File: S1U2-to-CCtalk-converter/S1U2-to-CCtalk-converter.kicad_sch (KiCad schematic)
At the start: 23 parts, among them J1 DB9_Female, J2 CCtalk Cable, J3 CCtalk Cable, Q1 BC847, Q2 BC856, U1 ST232B, U2 L7805

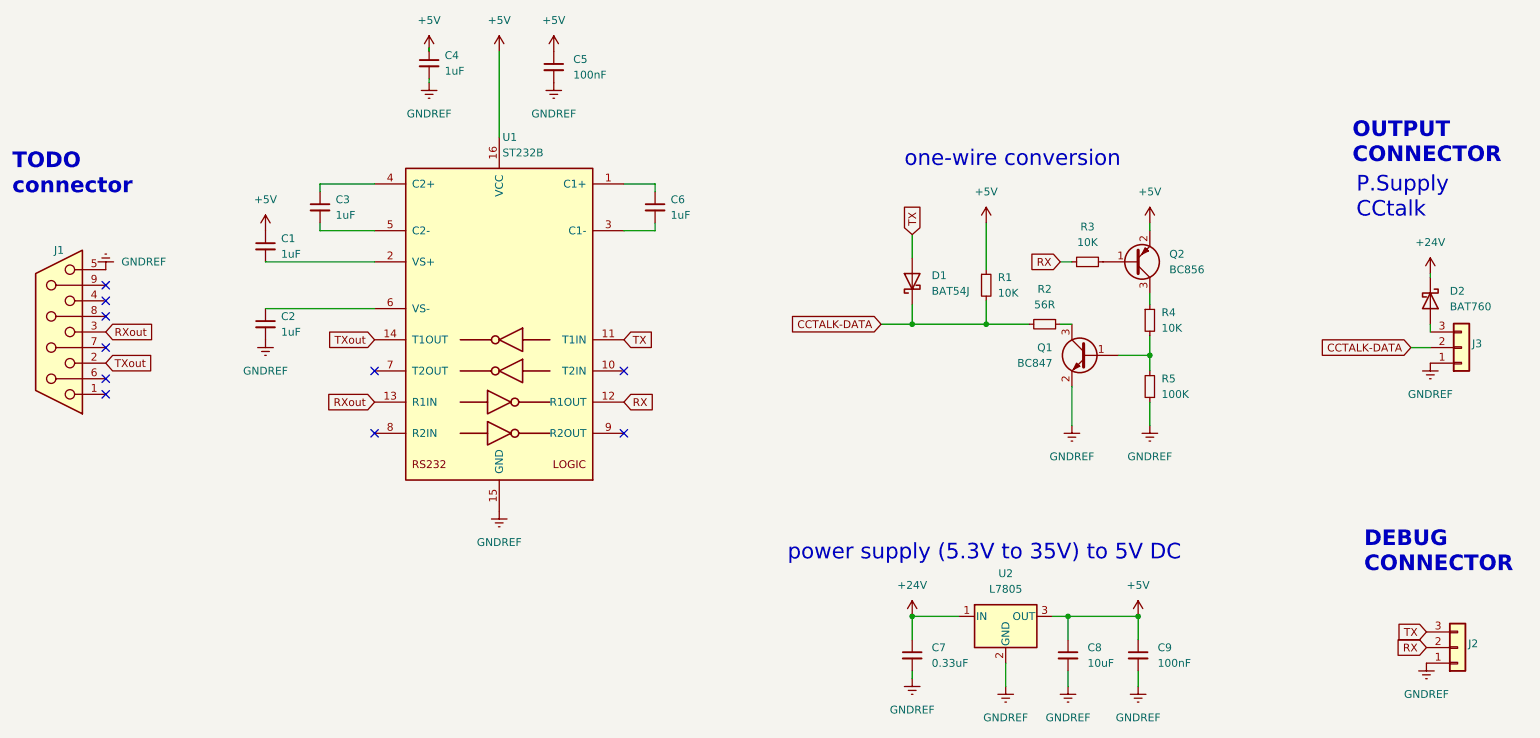
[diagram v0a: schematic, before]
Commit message: add s1u2 dxf bckg and place components
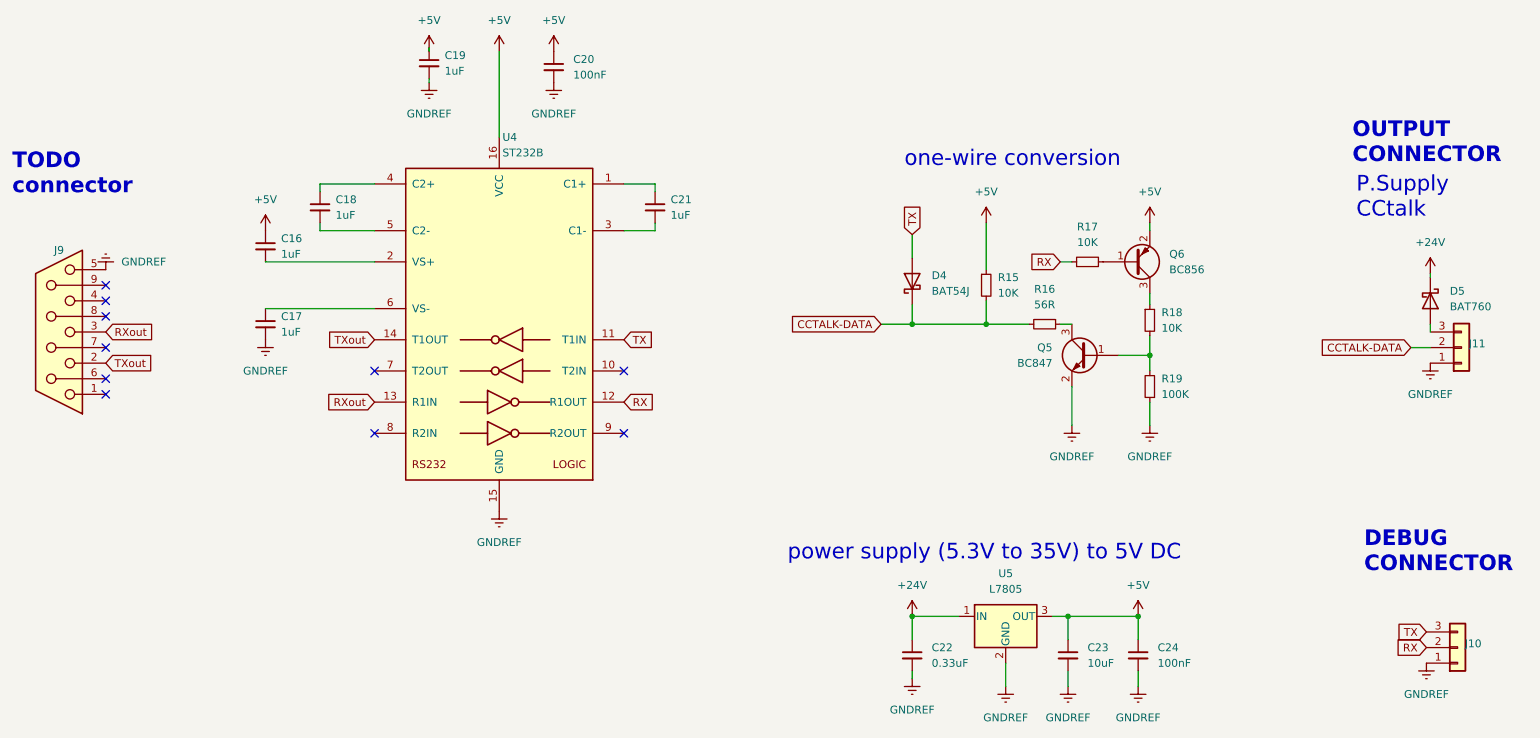
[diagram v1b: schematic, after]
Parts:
- renumbered C1 to C16, C2 to C17, C3 to C18, C4 to C19, C5 to C20, C6 to C21, C7 to C22, C8 to C23, C9 to C24, D1 to D4, D2 to D5, J2 to J10, J3 to J11, J1 to J9, Q1 to Q5, Q2 to Q6, R1 to R15, R2 to R16, R3 to R17, R4 to R18, R5 to R19, U1 to U4, U2 to U5
